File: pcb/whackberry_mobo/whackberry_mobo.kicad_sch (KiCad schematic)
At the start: 14 parts, among them SW1 SW_Omron_B3FS, SW2 SW_Omron_B3FS

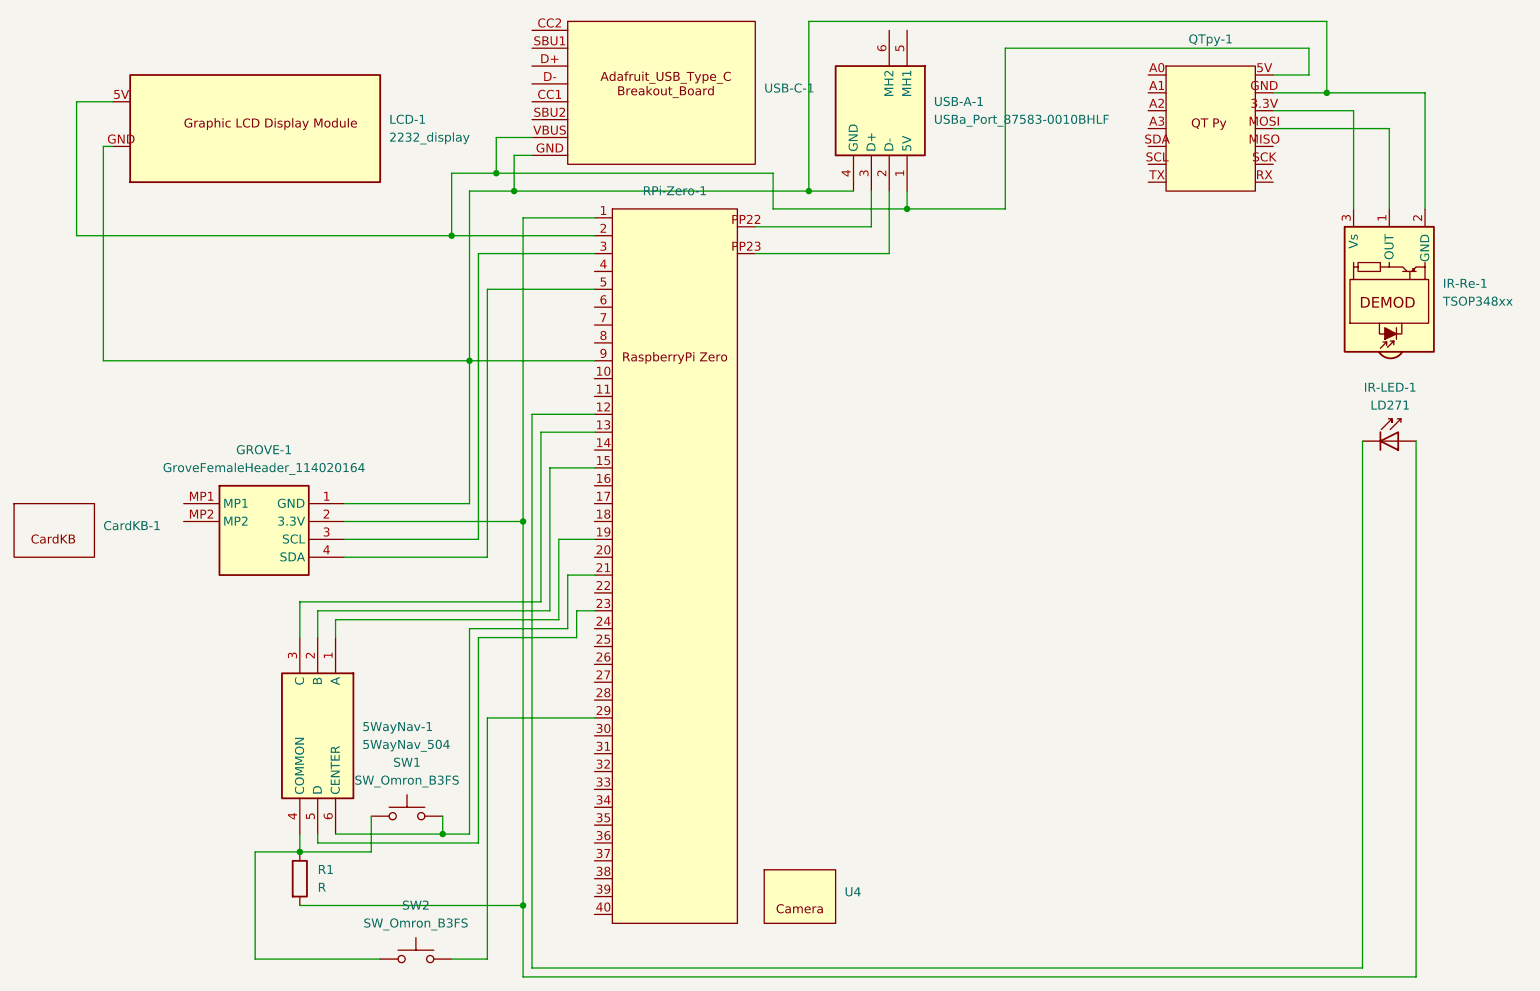
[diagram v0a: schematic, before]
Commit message: Adding a control switch for bridge power and other pcb improvements
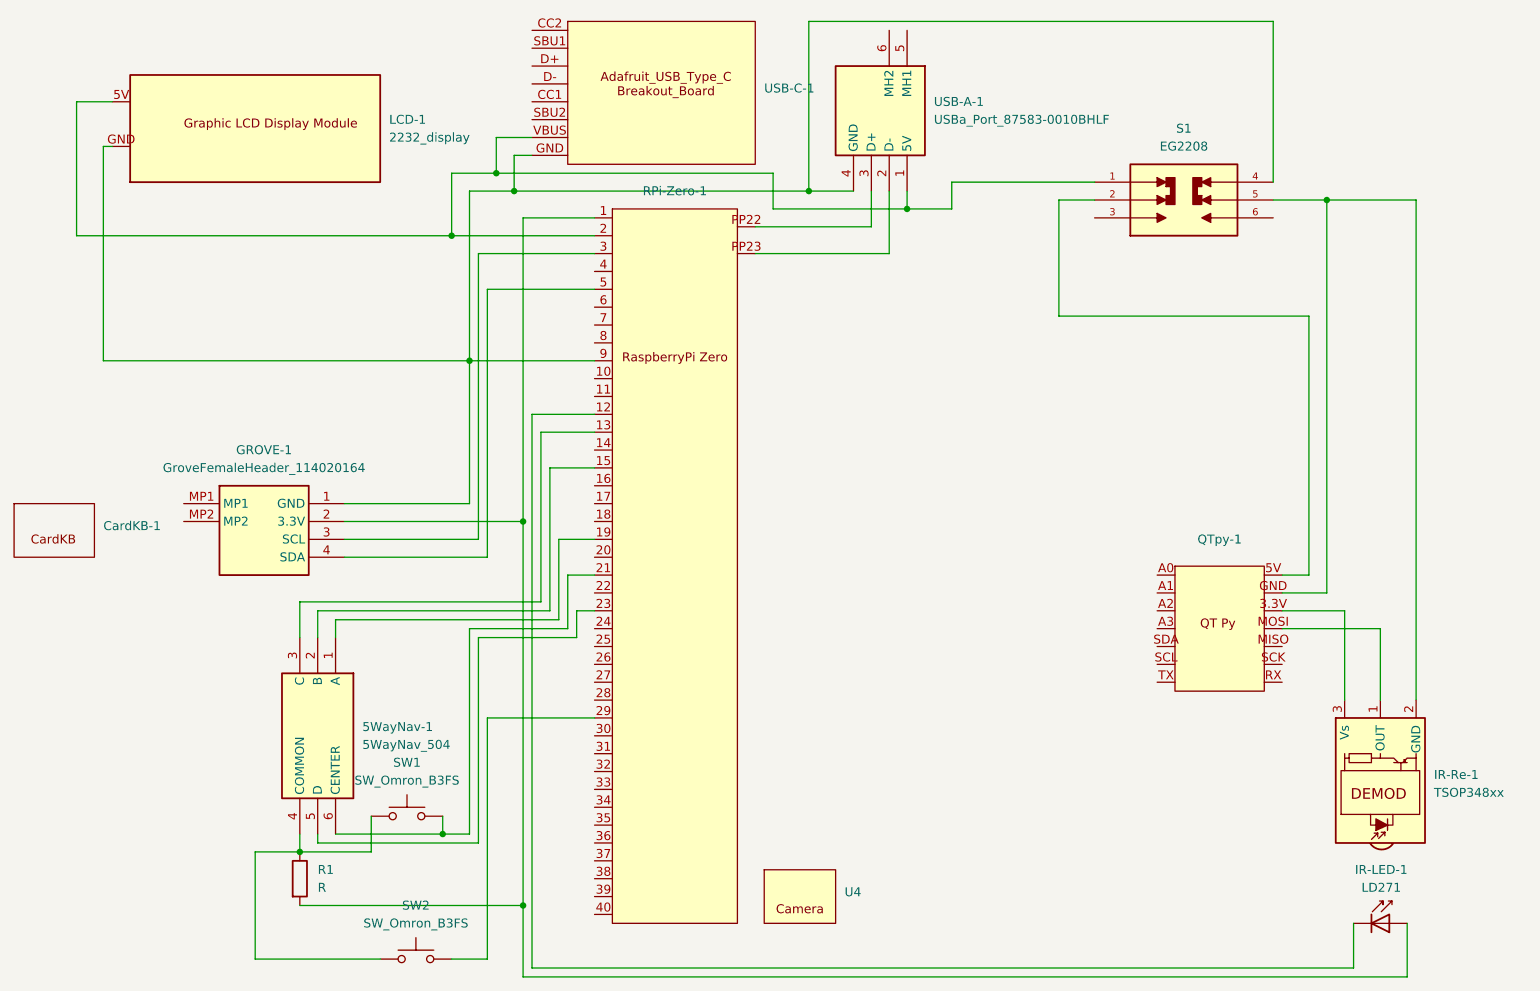
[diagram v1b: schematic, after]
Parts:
- added S1: EG2208, Whackberry_Parts_Library:SW_EG2208, symbol Whackberry_Symbols_Library:EG2208
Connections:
- net at LCD-1.5V, RPi-Zero-1.2, USB-A-1.1 (5V)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: now also S1.1; no longer QTpy-1.5V
- net at GROVE-1.1 (GND), LCD-1.GND, RPi-Zero-1.9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: now also S1.4; no longer IR-Re-1.2 (GND), QTpy-1.GND
- new net: IR-Re-1.2 (GND), QTpy-1.GND, S1.5
- new net: QTpy-1.5V, S1.2
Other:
- moved on the sheet: IR-LED-1, IR-Re-1, QTpy-1
